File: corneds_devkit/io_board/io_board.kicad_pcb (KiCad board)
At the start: 2 copper layers, 21.7 x 3.2 mm, 109 parts, among them J1 Conn_02x10_Counter_Clockwise, J2 JOYL_VSEL, J3 JOYR_VSEL, J4 nOEL_en, J5 nOER_en, SW1 SW_Push, SW10 SW_Push, SW11 SW_Push, SW12 SW_Push, SW13 SW_Push, SW14 SW_Push, SW15 SW_Push, SW16 SW_Push, SW17 SW_Push, SW18 SW_Push, SW19 SW_Push, SW2 SW_Push, SW20 SW_Push, SW21 SW_Push, SW22 SW_Push, SW23 SW_Push, SW24 SW_Push, SW25 SW_Push, SW26 SW_Push, SW27 SW_Push, SW28 SW_Push, SW29 SW_Push, SW3 SW_Push, SW30 SW_Push, SW31 SW_Push, SW32 SW_Push, SW33 SW_Push, SW34 SW_Push, SW35 SW_Push, SW36 SW_Push, SW37 SW_Push, SW38 SW_Push, SW39 SW_Push, SW4 SW_Push, SW40 SW_Push, SW41 SW_Push, SW42 SW_Push, SW43 SW_Push, SW44 SW_Push, SW5 SW_Push, SW6 SW_Push, SW7 SW_Push, SW8 SW_Push, SW9 SW_Push, U1 COM-09426, U2 COM-09426, U5 TXB0102DCU, U6 TXB0102DCU

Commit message: routing left keys pcb
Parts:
- SW1, SW10, SW11, SW12, SW13, SW14, SW15, SW16, SW17, SW18, SW19, SW2, SW20, SW21, SW22, SW23, SW24, SW25, SW26, SW27, SW28, SW29, SW3, SW30, SW31, SW32, SW33, SW34, SW35, SW36, SW37, SW38, SW39, SW4, SW40, SW41, SW42, SW43, SW44, SW5, SW6, SW7, SW8, SW9: footprint key-switches:SW_Gateron_LowProfile_HotSwap_THT -> key-switches:SW_Gateron_LowProfile_HotSwap_PTH
- moved J4 302.1 mm to (117.5, 50.0), turned to 90 degrees
- moved J2 298.5 mm to (127.5, 50.0), turned to -90 degrees
- moved J3 294.8 mm to (159.0, 50.0), turned to -90 degrees
- moved J5 294.7 mm to (166.0, 50.0), turned to -90 degrees
- moved U5 287.7 mm to (110.5, 53.0), turned to 90 degrees
- moved R10 284.7 mm to (169.5, 57.5), turned to 180 degrees
- moved R9 282.7 mm to (174.0, 57.5), turned to 180 degrees
- moved R8 279.3 mm to (169.5, 59.0), turned to 180 degrees
- moved J1 277.4 mm to (134.8, 55.3), turned to 90 degrees
- moved R7 277.2 mm to (174.0, 59.0)
- moved U1 271.5 mm to (116.0, 69.6), turned to 90 degrees
- moved U2 270.5 mm to (172.7, 69.6), turned to -90 degrees
- moved SW43 270.4 mm to (116.0, 91.1), turned to 90 degrees
- moved SW44 270.1 mm to (172.7, 91.1)
- moved D87 266.7 mm to (172.0, 85.4)
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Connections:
- D1 pad 4: left_led_di -> Net-(D1-DI)
- D11 pad 1: Net-(D10-DI) -> Net-(D11-DO)
- D11 pad 4: Net-(D11-DI) -> Net-(D10-DO)
- D12 pad 1: Net-(D11-DI) -> lclick_led_di
- D12 pad 4: Net-(D12-DI) -> Net-(D11-DO)
- D2 pad 1: Net-(D2-DO) -> Net-(D1-DI)
- D2 pad 4: Net-(D1-DO) -> Net-(D2-DI)
- D29 pad 1: Net-(D29-DO) -> Net-(D25-DI)
- D29 pad 4: Net-(D25-DO) -> Net-(D29-DI)
- D3 pad 1: Net-(D3-DO) -> Net-(D2-DI)
- D3 pad 4: Net-(D2-DO) -> Net-(D3-DI)
- D33 pad 1: Net-(D33-DO) -> Net-(D29-DI)
- D33 pad 4: Net-(D29-DO) -> Net-(D33-DI)
- D37 pad 1: Net-(D37-DO) -> Net-(D33-DI)
- D37 pad 4: Net-(D33-DO) -> Net-(D37-DI)
- D38 pad 1: lclick_led_di -> Net-(D38-DO)
- D38 pad 4: Net-(D38-DI) -> Net-(D25-DO)
- D4 pad 1: Net-(D4-DO) -> Net-(D3-DI)
- D4 pad 4: Net-(D3-DO) -> Net-(D4-DI)
- D41 pad 1: Net-(D41-DO) -> Net-(D37-DI)
- D41 pad 4: Net-(D37-DO) -> Net-(D41-DI)
- D42 pad 1: Net-(D38-DI) -> Net-(D42-DO)
- D42 pad 4: Net-(D42-DI) -> Net-(D38-DO)
- D45 pad 1: Net-(D45-DO) -> Net-(D41-DI)
- D45 pad 4: Net-(D41-DO) -> lclick_led_do
- D46 pad 1: Net-(D42-DI) -> unconnected-(D46-DO-Pad1)
- D46 pad 4: Net-(D45-DO) -> Net-(D42-DO)
- D5 pad 1: Net-(D5-DO) -> Net-(D4-DI)
- D5 pad 4: Net-(D4-DO) -> Net-(D5-DI)
- D6 pad 1: Net-(D12-DI) -> Net-(D5-DI)
- D6 pad 4: Net-(D5-DO) -> left_led_di
- D7 pad 1: Net-(D25-DI) -> Net-(D7-DO)
- D7 pad 4: Net-(D7-DI) -> Net-(D1-DO)
- D8 pad 1: Net-(D7-DI) -> Net-(D8-DO)
- D8 pad 4: Net-(D8-DI) -> Net-(D7-DO)
- D85 pad 1: unconnected-(D85-DO-Pad1) -> lclick_led_do
- D9 pad 1: Net-(D8-DI) -> Net-(D10-DI)
- D9 pad 4: Net-(D10-DO) -> Net-(D8-DO)
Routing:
- net VDD_5VL: track 0.00 -> 543.1 mm
- net COL2L: track 0.00 -> 226.7 mm, vias 0 -> 1
- net COL0L: track 0.00 -> 191.6 mm, vias 0 -> 1
- net COL1L: track 0.00 -> 181.7 mm, vias 0 -> 1
- net ROW0L: track 0.00 -> 179.2 mm, vias 0 -> 1
- net ROW1L: track 0.00 -> 168.2 mm, vias 0 -> 1
- net COL3L: track 0.00 -> 153.0 mm
- net ROW2L: track 0.00 -> 140.7 mm, vias 0 -> 1
- net ROW3L: track 0.00 -> 130.3 mm, vias 0 -> 1
- net COL4L: track 0.00 -> 129.3 mm
- net COL5L: track 0.00 -> 111.5 mm
- net VDD_3V3L: track 0.00 -> 93.3 mm, vias 0 -> 4
- net Net-(D25-DO): track 0.00 -> 93.3 mm
- net SCLL: track 0.00 -> 75.8 mm
- net nINTL: track 0.00 -> 70.8 mm, vias 0 -> 1
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- added copper zone on B.Cu, net GNDL
- added copper zone on F.Cu, net GNDL
- added copper zone on B.Cu, net GNDR
- added copper zone on F.Cu, net GNDR
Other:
- board size 21.7 x 3.2 mm -> 304 x 96.5 mm
- board text added: "JOYL_VSEL"
- board text added: "JOYR_VSEL"
- board text added: "nOEL_en"
- board text added: "nOER_en"

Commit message: finished io board
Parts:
- added REF**: MountingHole_3.2mm_M3_ISO7380_Pad_TopOnly, MountingHole:MountingHole_3.2mm_M3_ISO7380_Pad_TopOnly, F.Cu at (138.0, 96.2)
- added REF**: MountingHole_3.2mm_M3_ISO7380_Pad_TopOnly, MountingHole:MountingHole_3.2mm_M3_ISO7380_Pad_TopOnly, F.Cu at (150.0, 96.2)
- added REF**: MountingHole_3.2mm_M3_ISO7380_Pad_TopOnly, MountingHole:MountingHole_3.2mm_M3_ISO7380_Pad_TopOnly, F.Cu at (290.0, 138.5)
- added REF**: MountingHole_3.2mm_M3_ISO7380_Pad_TopOnly, MountingHole:MountingHole_3.2mm_M3_ISO7380_Pad_TopOnly, F.Cu at (290.0, 54.0)
- added REF**: MountingHole_3.2mm_M3_ISO7380_Pad_TopOnly, MountingHole:MountingHole_3.2mm_M3_ISO7380_Pad_TopOnly, F.Cu at (-2.00, 138.5)
- added REF**: MountingHole_3.2mm_M3_ISO7380_Pad_TopOnly, MountingHole:MountingHole_3.2mm_M3_ISO7380_Pad_TopOnly, F.Cu at (-2.00, 54.0)
- moved U6 50.5 mm to (172.7, 53.0), turned to -90 degrees
- moved R2 9.01 mm to (169.0, 111.5), turned to 90 degrees
- moved D87 7.69 mm to (177.8, 90.5), turned to 90 degrees
- moved J1 3.46 mm to (138.3, 55.3)
- moved J3 2.54 mm to (156.5, 50.0), turned to 90 degrees
- moved R10 1.00 mm to (169.5, 56.5)
- moved R7 1.00 mm to (174.0, 58.0), turned to 180 degrees
- moved R8 1.00 mm to (169.5, 58.0)
- moved R9 1.00 mm to (174.0, 56.5)
- moved D42 0.52 mm to (92.9, 119.2)
- moved D80 0.50 mm to (169.4, 127.8)
- moved D77 0.50 mm to (191.0, 57.2), turned to 180 degrees
- moved D78 0.50 mm to (191.0, 76.2)
- moved D79 0.50 mm to (191.0, 95.2), turned to 180 degrees
- moved D10 0.50 mm to (58.2, 71.4)
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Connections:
- D26 pad 4: right_led_di -> Net-(D26-DI)
- D28 pad 4: Net-(D28-DI) -> Net-(D26-DO)
- D30 pad 4: Net-(D28-DO) -> Net-(D30-DI)
- D49 pad 1: Net-(D49-DO) -> Net-(D26-DI)
- D49 pad 4: Net-(D26-DO) -> Net-(D49-DI)
- D50 pad 1: Net-(D28-DI) -> Net-(D50-DO)
- D50 pad 4: Net-(D50-DI) -> Net-(D28-DO)
- D51 pad 1: Net-(D51-DO) -> Net-(D30-DI)
- D51 pad 4: Net-(D30-DO) -> Net-(D51-DI)
- D55 pad 1: Net-(D55-DO) -> Net-(D49-DI)
- D55 pad 4: Net-(D49-DO) -> Net-(D55-DI)
- D56 pad 1: Net-(D50-DI) -> Net-(D56-DO)
- D56 pad 4: Net-(D56-DI) -> Net-(D50-DO)
- D57 pad 1: Net-(D57-DO) -> Net-(D51-DI)
- D57 pad 4: Net-(D51-DO) -> Net-(D57-DI)
- D61 pad 1: Net-(D61-DO) -> Net-(D55-DI)
- D61 pad 4: Net-(D55-DO) -> Net-(D61-DI)
- D62 pad 1: Net-(D56-DI) -> Net-(D62-DO)
- D62 pad 4: Net-(D62-DI) -> Net-(D56-DO)
- D63 pad 1: Net-(D63-DO) -> Net-(D57-DI)
- D63 pad 4: Net-(D57-DO) -> Net-(D63-DI)
- D64 pad 1: rclick_led_di -> Net-(D64-DO)
- D64 pad 4: Net-(D64-DI) -> Net-(D30-DO)
- D69 pad 1: Net-(D69-DO) -> Net-(D61-DI)
- D69 pad 4: Net-(D61-DO) -> Net-(D69-DI)
- D70 pad 1: Net-(D62-DI) -> Net-(D70-DO)
- D70 pad 4: Net-(D70-DI) -> Net-(D62-DO)
- D71 pad 1: Net-(D71-DO) -> Net-(D63-DI)
- D71 pad 4: Net-(D63-DO) -> Net-(D71-DI)
- D72 pad 1: Net-(D64-DI) -> Net-(D72-DO)
- D72 pad 4: Net-(D72-DI) -> Net-(D64-DO)
- D77 pad 1: Net-(D77-DO) -> Net-(D69-DI)
- D77 pad 4: Net-(D69-DO) -> right_led_di
- D78 pad 1: Net-(D70-DI) -> rclick_led_di
- D78 pad 4: Net-(D77-DO) -> Net-(D70-DO)
- D79 pad 1: Net-(D79-DO) -> Net-(D71-DI)
- D79 pad 4: Net-(D71-DO) -> rclick_led_do
- D80 pad 1: Net-(D72-DI) -> unconnected-(D80-DO-Pad1)
- D80 pad 4: Net-(D79-DO) -> Net-(D72-DO)
- D87 pad 1: unconnected-(D87-DO-Pad1) -> rclick_led_do
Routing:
- net VDD_5VR: track 0.00 -> 564.1 mm, vias 0 -> 4
- net ROW0R: track 0.00 -> 200.0 mm, vias 0 -> 1
- net ROW1R: track 0.00 -> 199.5 mm, vias 0 -> 1
- net COL0R: track 0.00 -> 166.3 mm
- net ROW2R: track 0.00 -> 164.7 mm, vias 0 -> 1
- net COL2R: track 0.00 -> 161.9 mm, vias 0 -> 1
- net COL1R: track 0.00 -> 148.1 mm
- net COL3R: track 0.00 -> 133.4 mm
- net COL4R: track 0.00 -> 115.6 mm
- net ROW3R: track 0.00 -> 108.7 mm, vias 0 -> 1
- net COL5R: track 0.00 -> 101.6 mm
- net VDD_3V3R: track 0.00 -> 100.8 mm, vias 0 -> 3
- net Net-(D30-DO): track 0.00 -> 93.4 mm
- net SDAR: track 0.00 -> 76.9 mm
- net nINTR: track 0.00 -> 72.5 mm, vias 0 -> 1
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
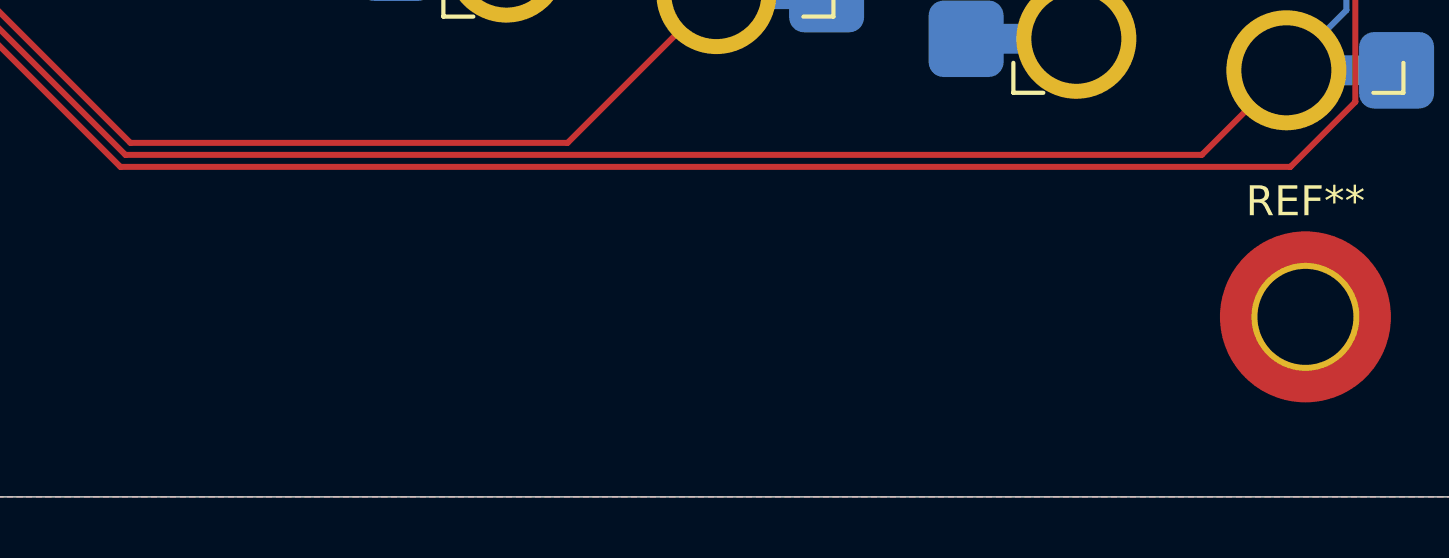
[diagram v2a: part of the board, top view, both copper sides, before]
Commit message: made power schematic and started on routing power board
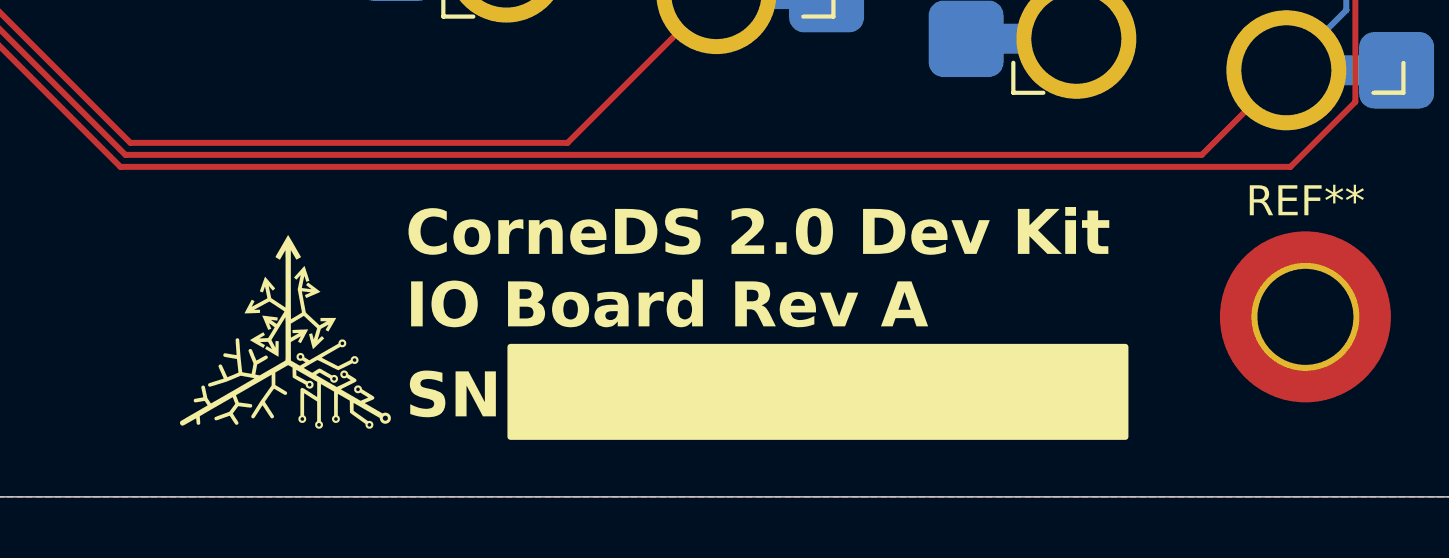
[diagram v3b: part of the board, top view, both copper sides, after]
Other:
- board text added: "CorneDS 2.0 Dev Kit IO Board Rev A"
- board text added: "Mar 13, 2025"
- board text added: "SN"

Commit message: finished routing power board and started on control board schematic but realized I need seperate reset lines
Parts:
- removed the REF** at (138.0, 96.2)
- removed the REF** at (150.0, 96.2)
- removed the REF** at (290.0, 138.5)
- removed the REF** at (290.0, 54.0)
- removed the REF** at (-2.00, 138.5)
- removed the REF** at (-2.00, 54.0)
- added REF**: MountingHole_3.2mm_M3_Pad_Via, MountingHole:MountingHole_3.2mm_M3_Pad_Via, F.Cu at (149.0, 96.5)
- added REF**: MountingHole_3.2mm_M3_Pad_Via, MountingHole:MountingHole_3.2mm_M3_Pad_Via, F.Cu at (289.0, 46.5)
- added REF**: MountingHole_3.2mm_M3_Pad_Via, MountingHole:MountingHole_3.2mm_M3_Pad_Via, F.Cu at (289.0, 146.5)
- added REF**: MountingHole_3.2mm_M3_Pad_Via, MountingHole:MountingHole_3.2mm_M3_Pad_Via, F.Cu at (139.0, 96.5)
- added REF**: MountingHole_3.2mm_M3_Pad_Via, MountingHole:MountingHole_3.2mm_M3_Pad_Via, F.Cu at (-1.00, 46.5)
- added REF**: MountingHole_3.2mm_M3_Pad_Via, MountingHole:MountingHole_3.2mm_M3_Pad_Via, F.Cu at (-1.00, 146.5)
- J1: footprint Connector_PinHeader_1.27mm:PinHeader_2x10_P1.27mm_Horizontal -> Connector_PinHeader_1.27mm:PinHeader_2x10_P1.27mm_Vertical
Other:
- board size 304 x 96.5 mm -> 304 x 114 mm

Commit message: ordered devkit rev A
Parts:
- removed D1, D10, D11, D12, D2, D25, D26, D28, D29, D3, D30, D33, D37, D38, D4, D41, D42, D45, D46, D49, D5, D50, D51, D55, D56, D57, D6, D61, D62, D63, D64, D69, D7, D70, D71, D72, D77, D78, D79, D8, D80, D85, D87, D9: SK68XX-SIDE, entropy:SK68XX-SIDE
- removed J3: JOYR_VSEL, Connector_PinHeader_1.27mm:PinHeader_1x03_P1.27mm_Vertical
- removed J4: nOEL_en, Connector_PinHeader_1.00mm:PinHeader_1x02_P1.00mm_Vertical
- removed J5: nOER_en, Connector_PinHeader_1.00mm:PinHeader_1x02_P1.00mm_Vertical
- removed R10, R8: 20k, Resistor_SMD:R_0402_1005Metric
- removed R2, R7, R9: 10k, Resistor_SMD:R_0402_1005Metric
- removed REF** (x6): MountingHole_3.2mm_M3_Pad_Via, MountingHole:MountingHole_3.2mm_M3_Pad_Via
- removed SW14, SW16, SW18, SW25, SW26, SW27, SW28, SW29, SW30, SW31, SW32, SW33, SW34, SW35, SW36, SW37, SW38, SW39, SW40, SW41, SW42, SW44: SW_Push, key-switches:SW_Gateron_LowProfile_HotSwap_PTH
- removed U2: COM-09426, entropy:COM-09426
- removed U4: ~, Package_DFN_QFN:WQFN-24-1EP_4x4mm_P0.5mm_EP2.45x2.45mm
- removed U5, U6: TXB0102DCU, Package_SO:VSSOP-8_2.4x2.1mm_P0.5mm
- added H1: MountingHole_Pad, MountingHole:MountingHole_3.2mm_M3_Pad_Via, F.Cu at (-5.00, 46.5)
- added H2: MountingHole_Pad, MountingHole:MountingHole_3.2mm_M3_Pad_Via, F.Cu at (125.0, 46.5)
- added H3: MountingHole_Pad, MountingHole:MountingHole_3.2mm_M3_Pad_Via, F.Cu at (-5.00, 146.5)
- added H4: MountingHole_Pad, MountingHole:MountingHole_3.2mm_M3_Pad_Via, F.Cu at (125.0, 146.5)
- added R12: 10k, Resistor_SMD:R_0402_1005Metric, F.Cu at (7.50, 48.0)
- J1: value Conn_02x10_Counter_Clockwise -> Conn_01x09_Pin; footprint Connector_PinHeader_1.27mm:PinHeader_2x10_P1.27mm_Vertical -> Connector_PinHeader_1.27mm:PinHeader_1x09_P1.27mm_Vertical; moved to B.Cu
- J2: value JOYL_VSEL -> JOY_VSEL
- moved R1 126.9 mm to (10.0, 50.5), turned to -135 degrees
- moved U3 124.0 mm to (6.61, 55.4)
- moved J1 81.2 mm to (57.8, 44.0), turned to -90 degrees
- moved J2 51.8 mm to (76.0, 44.0)
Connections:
- net COL0L renamed COL0
- net COL1L renamed COL1
- net COL2L renamed COL2
- net COL3L renamed COL3
- net COL4L renamed COL4
- net COL5L renamed COL5
- net ROW0L renamed ROW0
- net ROW1L renamed ROW1
- net ROW2L renamed ROW2
- net ROW3L renamed ROW3
- net VJOYL renamed VJOY
- net scroll_x renamed JOY_X
- net scroll_y renamed JOY_Y
- J1 pad 1: VDD_5VL -> GND
- J1 pad 2: VDD_3V3L -> nRESET
- J1 pad 4: nINTL -> Net-(J1-Pin_4)
- J1 pad 5: SDAL -> SCL
- J1 pad 6: SCLL -> SDA
- J1 pad 7: Net-(J1-Pin_7) -> nINT
- J1 pad 8: Net-(J1-Pin_8) -> VDD_3V3
- J1 pad 9: nRESET -> VDD_5V
- J2 pad 1: VDD_3V3L -> VDD_3V3
- J2 pad 3: VDD_5VL -> VDD_5V
- R1 pad 1: VDD_3V3L -> VDD_3V3
- R3 pad 2: Net-(J1-Pin_8) -> Net-(J1-Pin_3)
- R4 pad 1: Net-(J1-Pin_8) -> Net-(J1-Pin_3)
- R4 pad 2: GNDL -> GND
- R5 pad 2: Net-(J1-Pin_7) -> Net-(J1-Pin_4)
- R6 pad 1: Net-(J1-Pin_7) -> Net-(J1-Pin_4)
- R6 pad 2: GNDL -> GND
- U1 pad 4: GNDL -> GND
- U3 pad 19: GNDL -> GND
- U3 pad 21: VDD_3V3L -> VDD_3V3
- U3 pad 22: SDAL -> SDA
- U3 pad 23: SCLL -> SCL
- U3 pad 24: nINTL -> nINT
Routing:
- net VDD_5VL: track 584.4 -> 0.00 mm, vias 3 -> 0
- net VDD_5VR: track 564.1 -> 0.00 mm, vias 4 -> 0
- net ROW0R: track 200.0 -> 0.00 mm, vias 1 -> 0
- net ROW1R: track 199.5 -> 0.00 mm, vias 1 -> 0
- net COL0R: track 166.3 -> 0.00 mm
- net ROW2R: track 164.7 -> 0.00 mm, vias 1 -> 0
- net COL2R: track 161.9 -> 0.00 mm, vias 1 -> 0
- net ROW3: track 114.2 -> 262.5 mm, vias 2 -> 0
- net COL1R: track 148.1 -> 0.00 mm
- net VDD_3V3L: track 142.3 -> 0.00 mm, vias 4 -> 0
- net COL3R: track 133.4 -> 0.00 mm
- net VDD_3V3: track 0.00 -> 128.3 mm
- net COL4R: track 115.6 -> 0.00 mm
- net ROW3R: track 108.7 -> 0.00 mm, vias 1 -> 0
- net COL5R: track 101.6 -> 0.00 mm
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- added copper zone on B.Cu, net GND
- added copper zone on F.Cu, net GND
- removed copper zone on B.Cu, net GNDL
- removed copper zone on F.Cu, net GNDL
- removed copper zone on B.Cu, net GNDR
- removed copper zone on F.Cu, net GNDR
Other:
- board size 304 x 114 mm -> 144 x 114 mm
- board text added: "3.3V"
- board text added: "5V"
- board text added: "Apr 19, 2025"
- board text removed: "JOYL_VSEL"
- board text removed: "JOYR_VSEL"
- board text removed: "Mar 13, 2025"
- board text removed: "nOEL_en"
- board text removed: "nOER_en"
